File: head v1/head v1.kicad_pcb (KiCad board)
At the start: 2 copper layers, 40 x 35 mm, 31 parts, among them IC1 Con_I2C, J1 Conn_01x02, J2 Conn_01x02, J3 Conn_01x02, J4 Conn_01x02, J5 LIDAR, J6 Conn_01x02, J7 Conn_01x02

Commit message: fin routage head
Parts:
- C11, C13: moved to F.Cu
- D11, D12: moved to B.Cu
- moved J6 8.25 mm to (137.8, 50.8)
- moved J7 8.25 mm to (134.6, 58.4)
- moved DT3 5.08 mm to (132.1, 50.5)
- moved DT5 5.08 mm to (127.0, 50.5)
- moved R1 5.08 mm to (132.1, 53.0)
- moved R2 5.08 mm to (127.0, 53.0)
- moved R8 1.08 mm to (152.3, 53.8)
- moved C11 0.17 mm to (157.9, 71.5)
- moved C13 0.17 mm to (157.9, 65.4)
- moved D11 0.17 mm to (157.9, 65.4), turned to 180 degrees
- moved D12 0.17 mm to (157.9, 71.5), turned to 180 degrees
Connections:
- D11 pad 4: data -> LED
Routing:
- net GND: track 0.00 -> 151.0 mm, vias 0 -> 138
- net +3V3: track 0.00 -> 82.4 mm, vias 0 -> 3
- net +5VL: track 0.00 -> 51.2 mm, vias 0 -> 3
- net SDA: track 0.00 -> 43.8 mm, vias 0 -> 3
- net SCL: track 0.00 -> 36.0 mm, vias 0 -> 1
- net PWM: track 0.00 -> 31.5 mm
- net LED: track 0.00 -> 31.5 mm, vias 0 -> 1
- net RX: track 0.00 -> 30.0 mm, vias 0 -> 1
- net TX: track 0.00 -> 27.0 mm, vias 0 -> 1
- net Net-(ICM1-P0): track 0.00 -> 15.8 mm
- net Net-(ICM1-A2): track 0.00 -> 14.6 mm, vias 0 -> 2
- net tir: track 0.00 -> 13.7 mm
- net Net-(ICM1-A1): track 0.00 -> 11.8 mm, vias 0 -> 2
- net Net-(ICM1-A0): track 0.00 -> 10.2 mm, vias 0 -> 2
- net Net-(ICM1-P1): track 0.00 -> 9.65 mm
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- added copper zone on B.Cu, net GND
- added copper zone on F.Cu, net GND

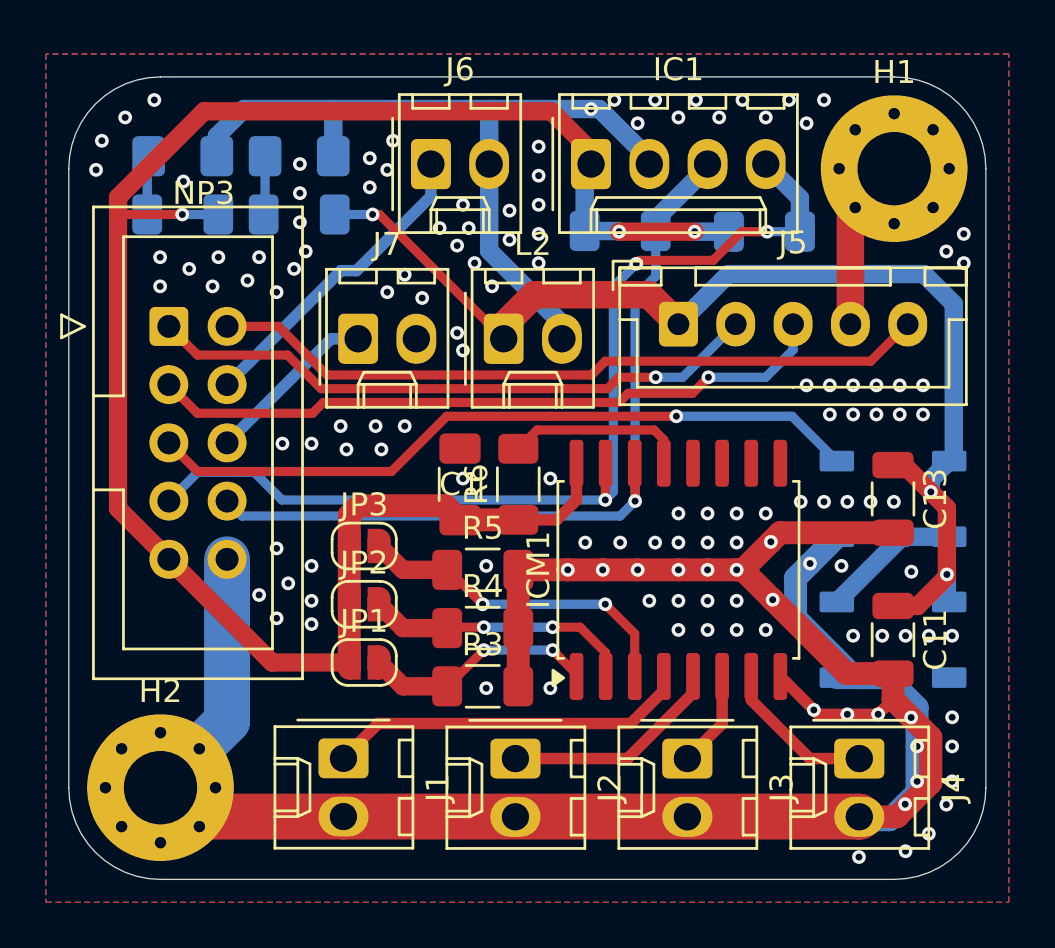
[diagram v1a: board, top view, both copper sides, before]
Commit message: fin routage head manque que la serigraphie
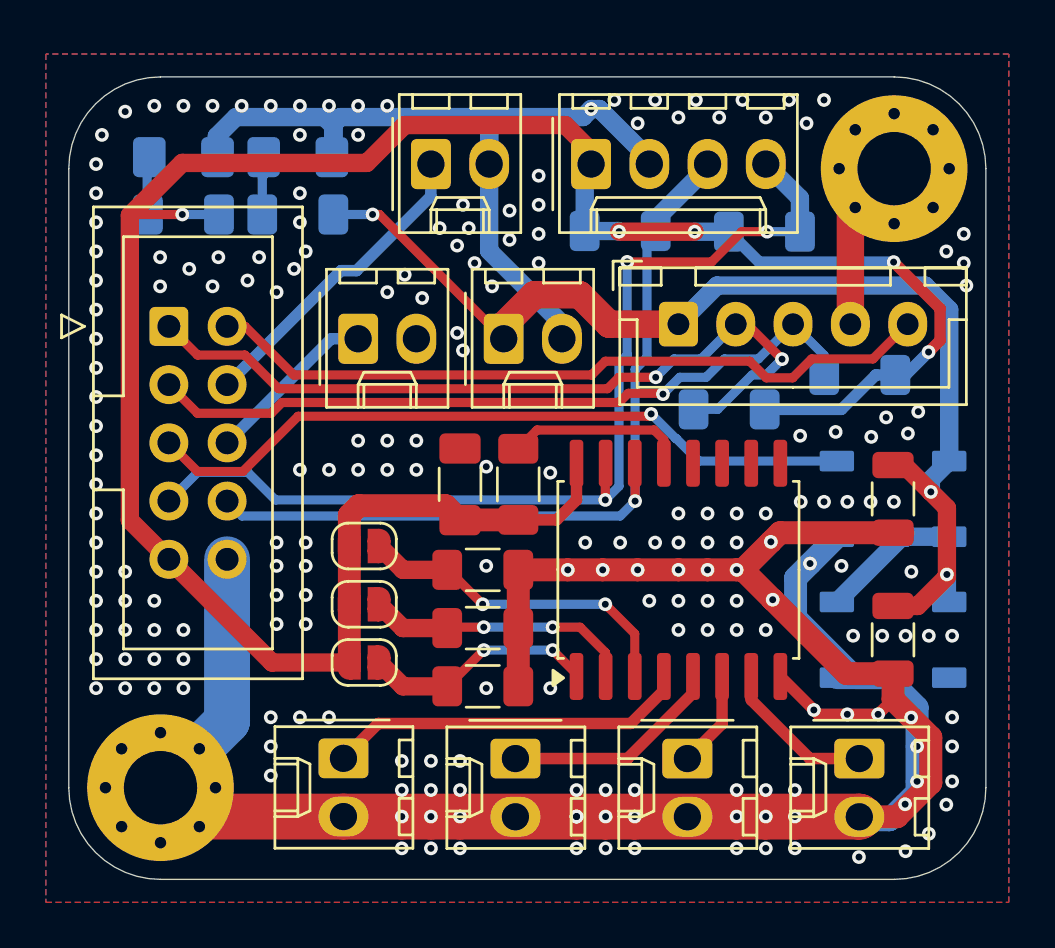
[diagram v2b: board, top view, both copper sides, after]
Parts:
- added R10: 4.7k, Resistor_SMD:R_1206_3216Metric_Pad1.30x1.75mm_HandSolder, B.Cu at (156.5, 60.0)
- added R9: 4.7k, Resistor_SMD:R_1206_3216Metric_Pad1.30x1.75mm_HandSolder, B.Cu at (150.8, 61.5)
- moved DT3 0.07 mm to (132.0, 50.5)
- moved R1 0.06 mm to (132.0, 53.0)
- moved DT5 0.05 mm to (127.0, 50.5)
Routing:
- net +3V3: track 82.4 -> 101.1 mm, vias 3 -> 5
- net TX: track 27.0 -> 34.4 mm, vias 1 -> 2
- net GND: track 151.0 -> 153.3 mm, vias 138 -> 205
- net RX: track 30.0 -> 32.2 mm
- net +5VL: track 51.2 -> 50.4 mm
- net PWM: track 31.5 -> 32.1 mm

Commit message: end head
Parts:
- added G***: LOGO, LOGO, B.Cu at (137.2, 56.8)
- added G***: LOGO, LOGO, B.Cu at (130.6, 68.0)
- added G***: LOGO, LOGO, B.Cu at (132.4, 79.2)
- added G***: LOGO, LOGO, B.Cu at (156.1, 56.0)
- added G***: LOGO, LOGO, B.Cu at (140.4, 49.2)
- added G***: LOGO, LOGO, B.Cu at (144.6, 55.5)
- added G***: LOGO, LOGO, B.Cu at (147.4, 49.0)
- added G***: LOGO, LOGO, B.Cu at (142.4, 54.5)
- added G***: LOGO, LOGO, B.Cu at (143.4, 56.6)
- added G***: LOGO, LOGO, B.Cu at (127.6, 71.8)
- added kibuzzard-69B7FFCA: G***, kibuzzard-69B7FFCA, F.Cu at (134.2, 51.0)
- added kibuzzard-69B800EA: G***, kibuzzard-69B800EA, F.Cu at (134.2, 54.1)
- added kibuzzard-69B800EA: G***, kibuzzard-69B800EA, B.Cu at (131.2, 60.7)
- added kibuzzard-69BAE0CF: G***, kibuzzard-69BAE0CF, F.Cu at (155.6, 65.4)
- added kibuzzard-69BAE0CF: G***, kibuzzard-69BAE0CF, F.Cu at (155.6, 71.5)
- added kibuzzard-69BAE350: G***, kibuzzard-69BAE350, B.Cu at (135.8, 60.6)
- added kibuzzard-69BAE75D: G***, kibuzzard-69BAE75D, B.Cu at (149.9, 48.4)
- added kibuzzard-69BAE766: G***, kibuzzard-69BAE766, B.Cu at (152.4, 48.4)
- added kibuzzard-69BAE8DD: G***, kibuzzard-69BAE8DD, B.Cu at (131.2, 57.6)
- added kibuzzard-69BAED5C: G***, kibuzzard-69BAED5C, B.Cu at (151.0, 55.8)
- added kibuzzard-69BAED6C: G***, kibuzzard-69BAED6C, B.Cu at (153.6, 55.8)
- added kibuzzard-69BAED73: G***, kibuzzard-69BAED73, B.Cu at (158.6, 55.8)
- added kibuzzard-69BAED80: G***, kibuzzard-69BAED80, B.Cu at (139.0, 53.0)
- added kibuzzard-69C6521F: G***, kibuzzard-69C6521F, B.Cu at (143.4, 73.8)
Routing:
- net GND: track 153.3 -> 145.1 mm, vias 205 -> 211
- net +3V3: track 101.1 -> 99.3 mm
- net SDA: track 44.1 -> 45.2 mm
